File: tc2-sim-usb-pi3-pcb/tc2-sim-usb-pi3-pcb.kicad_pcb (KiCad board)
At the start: 4 copper layers, 22.5 x 28 mm, 5 parts, among them J1 Conn_01x08, J2 Conn_01x03

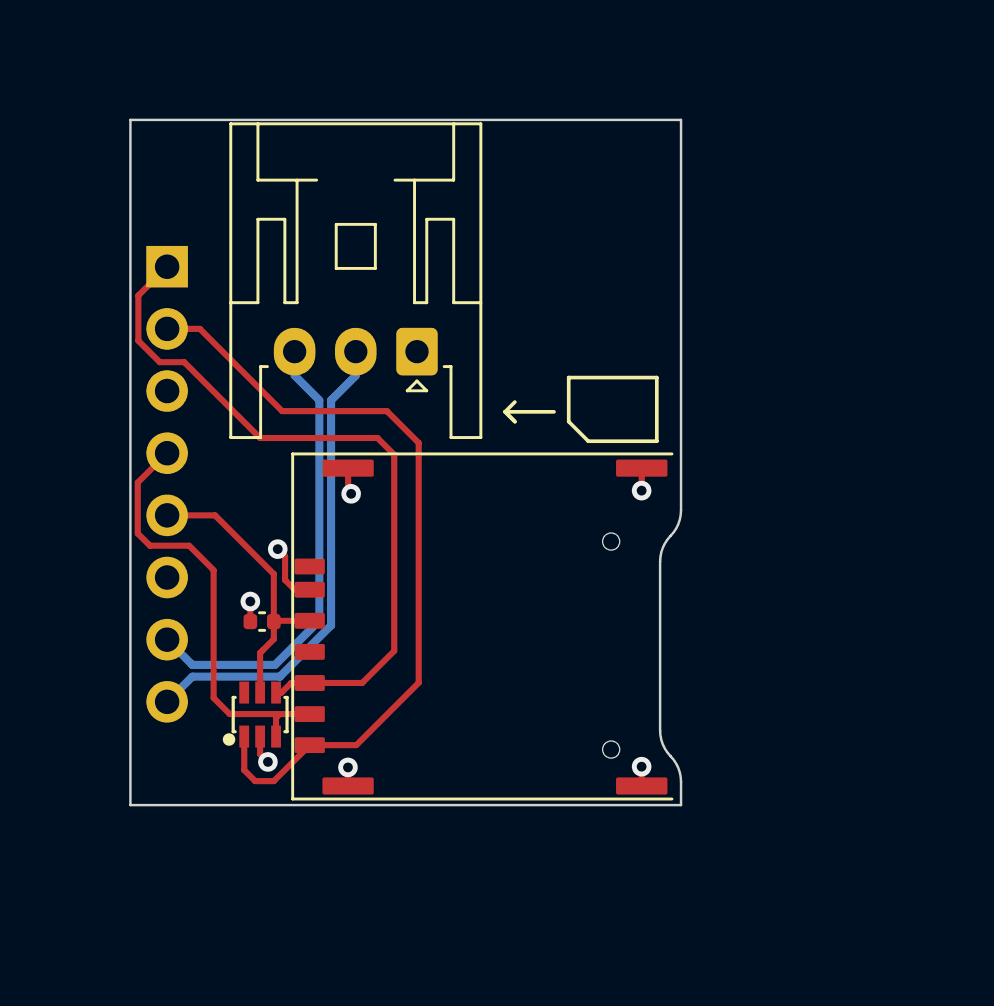
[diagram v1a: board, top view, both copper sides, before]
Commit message: Add JLPCPCB 2D barcode to PCBs
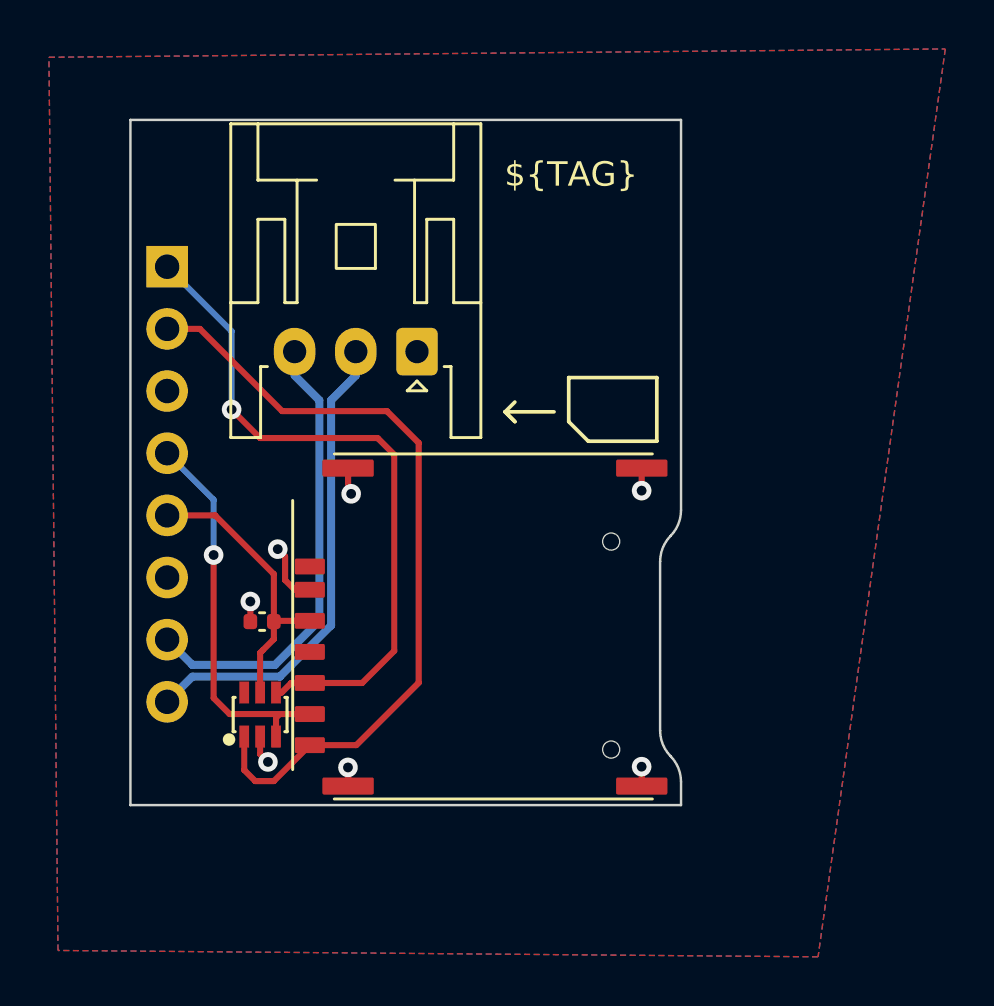
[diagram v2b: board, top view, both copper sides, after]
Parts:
- added U2: ~, cacophony-library:JLCPCB_QR_8mm, B.Cu at (12.0, 15.0)
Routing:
- net USIM_DATA: track 17.9 -> 16.0 mm, vias 0 -> 1
- net USIM_RST: track 29.5 -> 27.7 mm, vias 0 -> 1
- added copper zone on B.Cu, net GND
- added copper zone on F.Cu, net GND
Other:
- board text added: "${TAG}"

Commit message: Add git hash to PCBs
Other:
- board text added: "${HASH}"
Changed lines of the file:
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@@
 		(layer "Edge.Cuts")
+	)
+	(gr_text "${HASH}"
+		(at 13.48 0.8 0)
+		(layer "F.SilkS")
+		(effects
+			(font
+				(size 1 1)
+				(thickness 0.15)
+			)
+			(justify left bottom)
+		)
 	)
 	(gr_text "${TAG}"

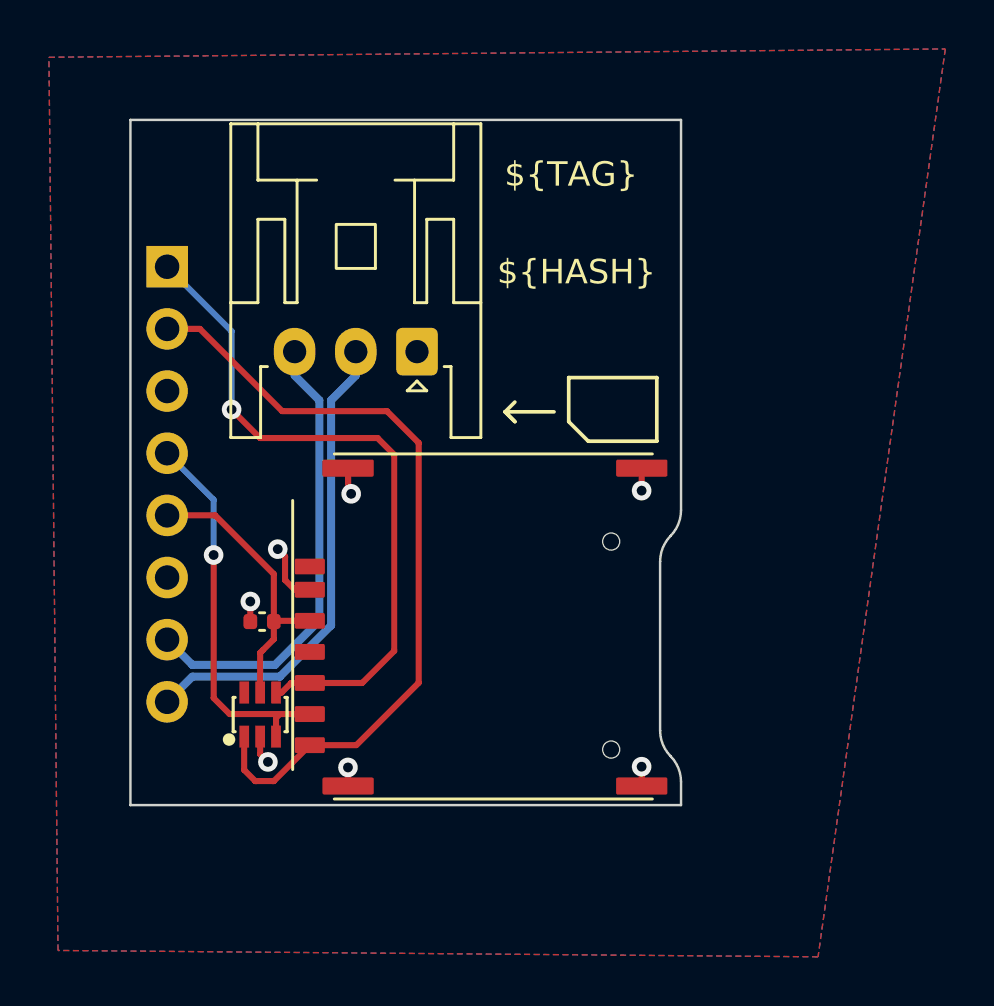
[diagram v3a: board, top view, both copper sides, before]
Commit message: Add panel for tc2-sim-usb-pi3
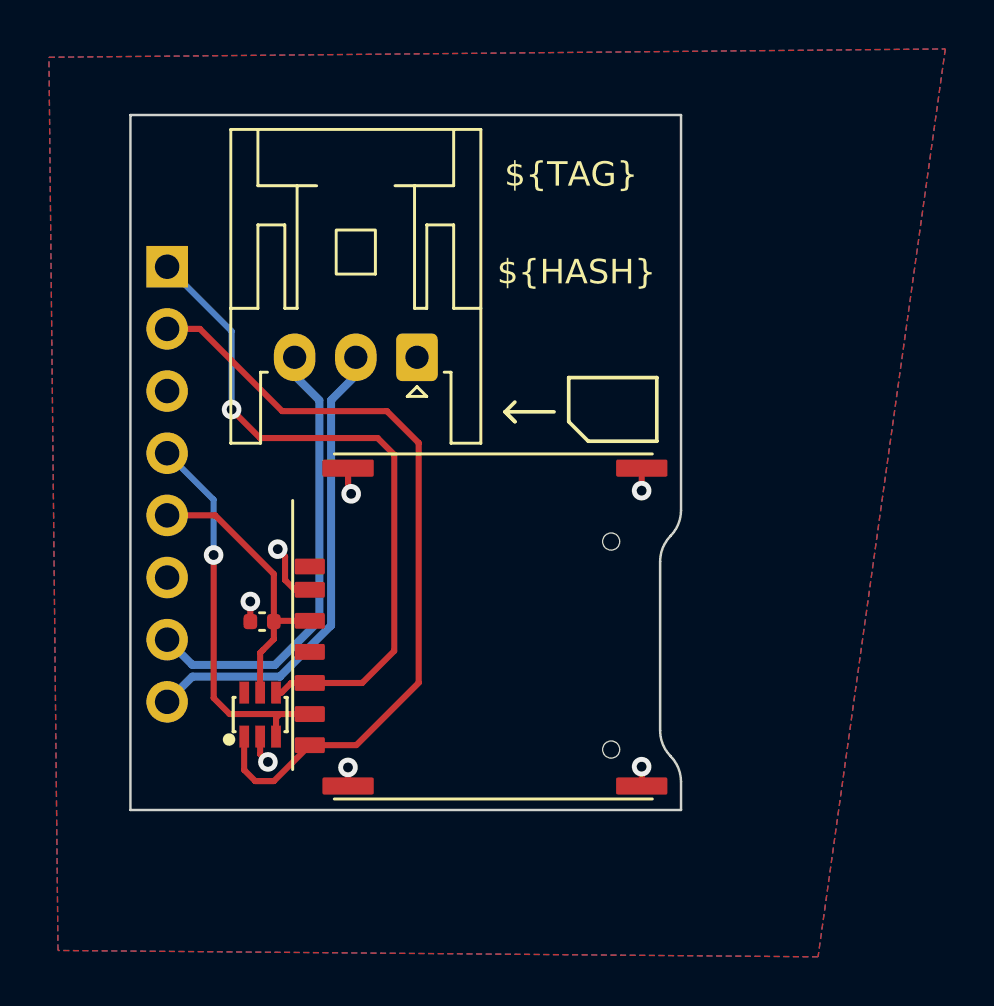
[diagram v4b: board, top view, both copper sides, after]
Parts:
- added REF**: Tab, PCM_kikit:Tab, F.Cu at (9.75, -6.49)
- added REF**: Tab, PCM_kikit:Tab, F.Cu at (21.3, 0.76)
- added REF**: Tab, PCM_kikit:Tab, F.Cu at (9.75, 22.4)
- added REF**: Tab, PCM_kikit:Tab, F.Cu at (-1.95, 8.00)
- moved J2 0.23 mm to (10.2, 3.70)
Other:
- board size 22.5 x 28 mm -> 22.5 x 28.4 mm
